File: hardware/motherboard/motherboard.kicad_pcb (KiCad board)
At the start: 2 copper layers, 22 parts, among them J1 Conn_01x02, J2 Conn_02x03_Odd_Even, U1 ESP32-WROOM-32, U2 SHTC3, U3 BMP390, U4 TPS62177DQC, U8 NRF24L01_Breakout

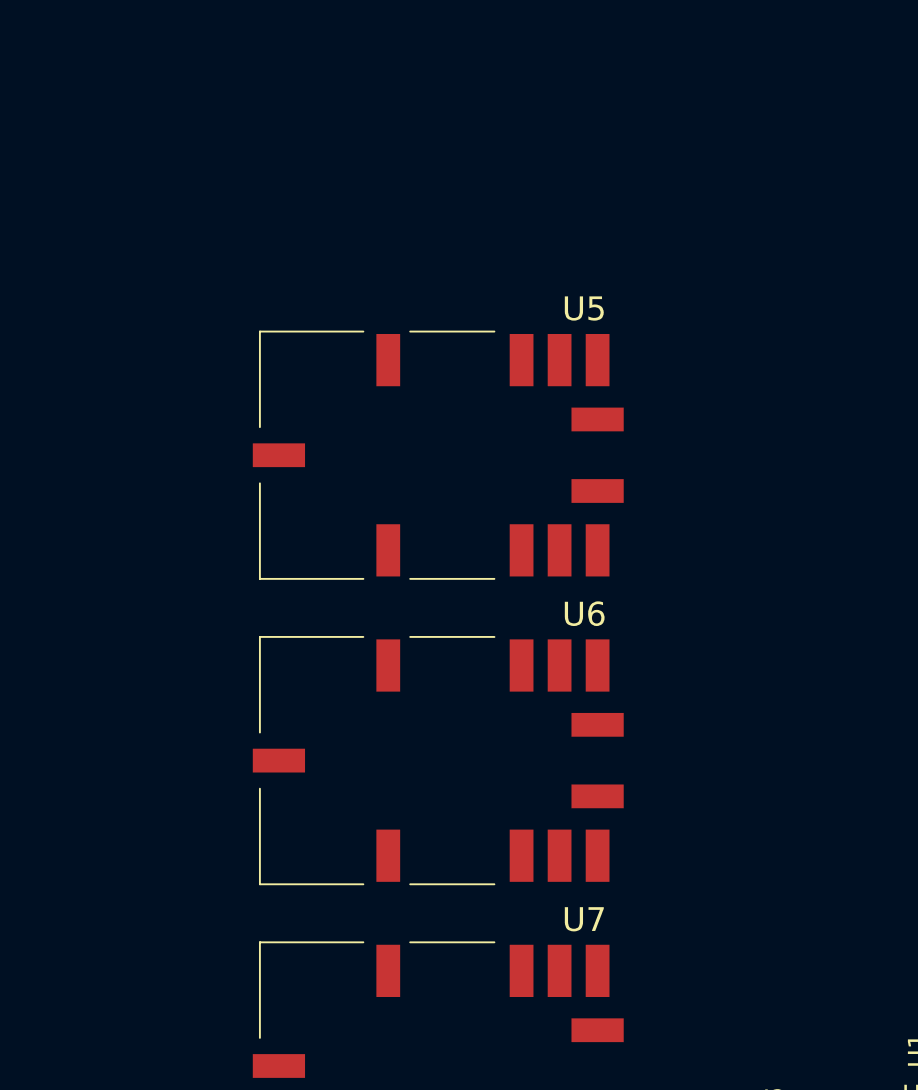
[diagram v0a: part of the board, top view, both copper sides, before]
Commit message: Completed schematic
Completed schematic with all footprints assigned
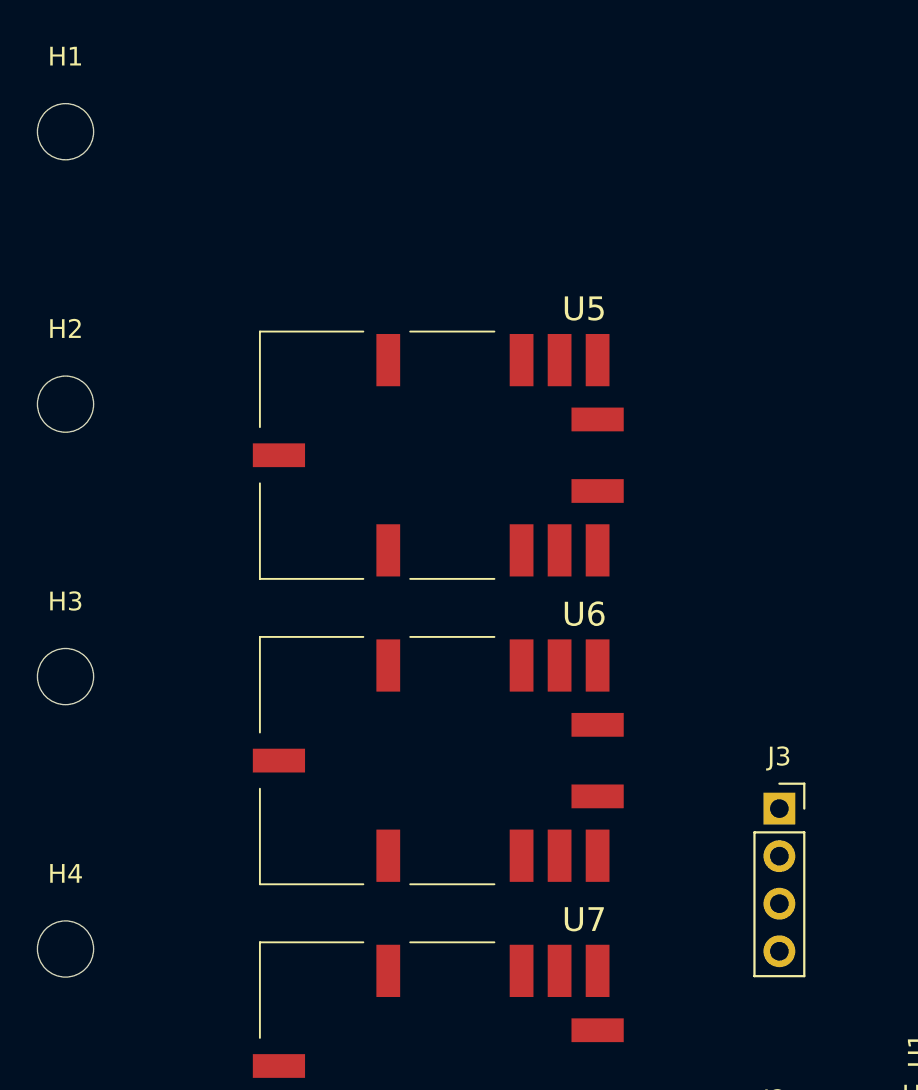
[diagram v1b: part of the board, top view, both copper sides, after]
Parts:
- added H1: MountingHole, MountingHole:MountingHole_3mm, F.Cu at (94.0, 59.1)
- added H2: MountingHole, MountingHole:MountingHole_3mm, F.Cu at (94.0, 73.7)
- added H3: MountingHole, MountingHole:MountingHole_3mm, F.Cu at (94.0, 88.2)
- added H4: MountingHole, MountingHole:MountingHole_3mm, F.Cu at (94.0, 102.8)
- added J3: Conn_01x04, Connector_PinSocket_2.54mm:PinSocket_1x04_P2.54mm_Vertical, F.Cu at (132.1, 95.3)
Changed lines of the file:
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@@
   (net 63 "unconnected-(U7-DNC-Pad7)")
   (net 64 "Net-(J1-Pin_2)")
+  (footprint "MountingHole:MountingHole_3mm" (layer "F.Cu")
+    (at 93.98 73.66)
+    (descr "Mounting Hole 3mm, no annular")
+    (tags "mounting hole 3mm no annular")
+    (property "Sheetfile" "motherboard.kicad_sch")
+    (property "Sheetname" "")
+    (property "ki_description" "Mounting Hole without connection")
+    (property "ki_keywords" "mounting hole")
+    (attr exclude_from_pos_files)
+    (fp_text reference "H2" (at 0 -4) (layer "F.SilkS")
+        (effects (font (size 1 1) (thickness 0.15)))
+    )
+    (fp_text value "MountingHole" (at 0 4) (layer "F.Fab")
+        (effects (font (size 1 1) (thickness 0.15)))
+    )
+    (fp_text user "${REFERENCE}" (at 0 0) (layer "F.Fab")
+        (effects (font (size 1 1) (thickness 0.15)))
+    )
+    (fp_circle (center 0 0) (end 3 0)
+      (stroke (width 0.15) (type solid)) (fill none) (layer "Cmts.User"))
+    (fp_circle (center 0 0) (end 3.25 0)
+      (stroke (width 0.05) (type solid)) (fill none) (layer "F.CrtYd"))
+    (pad "" np_thru_hole circle (at 0 0) (size 3 3) (drill 3) (layers "*.Cu" "*.Mask"))
+  )
   (footprint "Connector_IDC:IDC-Header_2x03_P2.54mm_Vertical" (layer "F.Cu")
     (at 130.5818 116.897874)
@@
       ))
   )
+  (footprint "Connector_PinSocket_2.54mm:PinSocket_1x04_P2.54mm_Vertical" (layer "F.Cu")
+    (at 132.105 95.26)
+    (descr "Through hole straight socket strip, 1x04, 2.54mm pitch, single row (from Kicad 4.0.7), script generated")
+    (tags "Through hole socket strip THT 1x04 2.54mm single row")
+    (property "Sheetfile" "motherboard.kicad_sch")
+    (property "Sheetname" "")
+    (property "ki_description" "Generic connector, single row, 01x04, script generated (kicad-library-utils/schlib/autogen/connector/)")
+    (property "ki_keywords" "connector")
+    (attr through_hole)
+    (fp_text reference "J3" (at 0 -2.77) (layer "F.SilkS")
+        (effects (font (size 1 1) (thickness 0.15)))
+    )
+    (fp_text value "Conn_01x04" (at 0 10.39) (layer "F.Fab")
+        (effects (font (size 1 1) (thickness 0.15)))
+    )
+    (fp_text user "${REFERENCE}" (at 0 3.81 90) (layer "F.Fab")
+        (effects (font (size 1 1) (thickness 0.15)))
+    )
+    (fp_line (start -1.33 1.27) (end -1.33 8.95)
+      (stroke (width 0.12) (type solid)) (layer "F.SilkS"))
+    (fp_line (start -1.33 1.27) (end 1.33 1.27)
+      (stroke (width 0.12) (type solid)) (layer "F.SilkS"))
+    (fp_line (start -1.33 8.95) (end 1.33 8.95)
+      (stroke (width 0.12) (type solid)) (layer "F.SilkS"))
+    (fp_line (start 0 -1.33) (end 1.33 -1.33)
+      (stroke (width 0.12) (type solid)) (layer "F.SilkS"))
+    (fp_line (start 1.33 -1.33) (end 1.33 0)
+      (stroke (width 0.12) (type solid)) (layer "F.SilkS"))
+    (fp_line (start 1.33 1.27) (end 1.33 8.95)
+      (stroke (width 0.12) (type solid)) (layer "F.SilkS"))
+    (fp_line (start -1.8 -1.8) (end 1.75 -1.8)
+      (stroke (width 0.05) (type solid)) (layer "F.CrtYd"))
+    (fp_line (start -1.8 9.4) (end -1.8 -1.8)
+      (stroke (width 0.05) (type solid)) (layer "F.CrtYd"))
+    (fp_line (start 1.75 -1.8) (end 1.75 9.4)
+      (stroke (width 0.05) (type solid)) (layer "F.CrtYd"))
+    (fp_line (start 1.75 9.4) (end -1.8 9.4)
+      (stroke (width 0.05) (type solid)) (layer "F.CrtYd"))
+    (fp_line (start -1.27 -1.27) (end 0.635 -1.27)
+      (stroke (width 0.1) (type solid)) (layer "F.Fab"))
+    (fp_line (start -1.27 8.89) (end -1.27 -1.27)
+      (stroke (width 0.1) (type solid)) (layer "F.Fab"))
+    (fp_line (start 0.635 -1.27) (end 1.27 -0.635)
+      (stroke (width 0.1) (type solid)) (layer "F.Fab"))
+    (fp_line (start 1.27 -0.635) (end 1.27 8.89)
+      (stroke (width 0.1) (type solid)) (layer "F.Fab"))
+    (fp_line (start 1.27 8.89) (end -1.27 8.89)
+      (stroke (width 0.1) (type solid)) (layer "F.Fab"))
+    (pad "1" thru_hole rect (at 0 0) (size 1.7 1.7) (drill 1) (layers "*.Cu" "*.Mask")
+      (net 1 "GND") (pinfunction "Pin_1") (pintype "passive"))
+    (pad "2" thru_hole oval (at 0 2.54) (size 1.7 1.7) (drill 1) (layers "*.Cu" "*.Mask")
+      (net 3 "+3.3V") (pinfunction "Pin_2") (pintype "passive"))
+    (pad "3" thru_hole oval (at 0 5.08) (size 1.7 1.7) (drill 1) (layers "*.Cu" "*.Mask")
+      (net 48 "/SDA") (pinfunction "Pin_3") (pintype "passive"))
+    (pad "4" thru_hole oval (at 0 7.62) (size 1.7 1.7) (drill 1) (layers "*.Cu" "*.Mask")
+      (net 49 "/SCL") (pinfunction "Pin_4") (pintype "passive"))
+    (model "${KICAD6_3DMODEL_DIR}/Connector_PinSocket_2.54mm.3dshapes/PinSocket_1x04_P2.54mm_Vertical.wrl"
+      (offset (xyz 0 0 0))
+      (scale (xyz 1 1 1))
+      (rotate (xyz 0 0 0))
+    )
+  )
   (footprint "Jumper:SolderJumper-2_P1.3mm_Open_RoundedPad1.0x1.5mm" (layer "F.Cu")
     (at 113.3068 126.037874)
@@
       ))
   )
+  (footprint "MountingHole:MountingHole_3mm" (layer "F.Cu")
+    (at 93.98 102.76)
+    (descr "Mounting Hole 3mm, no annular")
+    (tags "mounting hole 3mm no annular")
+    (property "Sheetfile" "motherboard.kicad_sch")
+    (property "Sheetname" "")
+    (property "ki_description" "Mounting Hole without connection")
+    (property "ki_keywords" "mounting hole")
+    (attr exclude_from_pos_files)
+    (fp_text reference "H4" (at 0 -4) (layer "F.SilkS")
+        (effects (font (size 1 1) (thickness 0.15)))
+    )
+    (fp_text value "MountingHole" (at 0 4) (layer "F.Fab")
+        (effects (font (size 1 1) (thickness 0.15)))
+    )
+    (fp_text user "${REFERENCE}" (at 0 0) (layer "F.Fab")
+        (effects (font (size 1 1) (thickness 0.15)))
+    )
+    (fp_circle (center 0 0) (end 3 0)
+      (stroke (width 0.15) (type solid)) (fill none) (layer "Cmts.User"))
+    (fp_circle (center 0 0) (end 3.25 0)
+      (stroke (width 0.05) (type solid)) (fill none) (layer "F.CrtYd"))
+    (pad "" np_thru_hole circle (at 0 0) (size 3 3) (drill 3) (layers "*.Cu" "*.Mask"))
+  )
   (footprint "Connector_AMASS:AMASS_XT60-F_1x02_P7.20mm_Vertical" (layer "F.Cu")
     (at 142.4968 132.697874)
@@
       (rotate (xyz 0 0 0))
     )
+  )
+  (footprint "MountingHole:MountingHole_3mm" (layer "F.Cu")
+    (at 93.98 88.21)
+    (descr "Mounting Hole 3mm, no annular")
+    (tags "mounting hole 3mm no annular")
+    (property "Sheetfile" "motherboard.kicad_sch")
+    (property "Sheetname" "")
+    (property "ki_description" "Mounting Hole without connection")
+    (property "ki_keywords" "mounting hole")
+    (attr exclude_from_pos_files)
+    (fp_text reference "H3" (at 0 -4) (layer "F.SilkS")
+        (effects (font (size 1 1) (thickness 0.15)))
+    )
+    (fp_text value "MountingHole" (at 0 4) (layer "F.Fab")
+        (effects (font (size 1 1) (thickness 0.15)))
+    )
+    (fp_text user "${REFERENCE}" (at 0 0) (layer "F.Fab")
+        (effects (font (size 1 1) (thickness 0.15)))
+    )
+    (fp_circle (center 0 0) (end 3 0)
+      (stroke (width 0.15) (type solid)) (fill none) (layer "Cmts.User"))
+    (fp_circle (center 0 0) (end 3.25 0)
+      (stroke (width 0.05) (type solid)) (fill none) (layer "F.CrtYd"))
+    (pad "" np_thru_hole circle (at 0 0) (size 3 3) (drill 3) (layers "*.Cu" "*.Mask"))
   )
   (footprint "RF_Module:ESP32-WROOM-32D" (layer "F.Cu")
@@
       ))
   )
+  (footprint "MountingHole:MountingHole_3mm" (layer "F.Cu")
+    (at 93.98 59.11)
+    (descr "Mounting Hole 3mm, no annular")
+    (tags "mounting hole 3mm no annular")
+    (property "Sheetfile" "motherboard.kicad_sch")
+    (property "Sheetname" "")
+    (property "ki_description" "Mounting Hole without connection")
+    (property "ki_keywords" "mounting hole")
+    (attr exclude_from_pos_files)
+    (fp_text reference "H1" (at 0 -4) (layer "F.SilkS")
+        (effects (font (size 1 1) (thickness 0.15)))
+    )
+    (fp_text value "MountingHole" (at 0 4) (layer "F.Fab")
+        (effects (font (size 1 1) (thickness 0.15)))
+    )
+    (fp_text user "${REFERENCE}" (at 0 0) (layer "F.Fab")
+        (effects (font (size 1 1) (thickness 0.15)))
+    )
+    (fp_circle (center 0 0) (end 3 0)
+      (stroke (width 0.15) (type solid)) (fill none) (layer "Cmts.User"))
+    (fp_circle (center 0 0) (end 3.25 0)
+      (stroke (width 0.05) (type solid)) (fill none) (layer "F.CrtYd"))
+    (pad "" np_thru_hole circle (at 0 0) (size 3 3) (drill 3) (layers "*.Cu" "*.Mask"))
+  )
   (footprint "RF_Module:nRF24L01_Breakout" (layer "F.Cu")

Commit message: Initial PCB design
Initial PCB design complete
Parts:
- added C1: 100n, Capacitor_SMD:C_0603_1608Metric, F.Cu at (142.6, 121.6)
- added C10: 100n, Capacitor_SMD:C_0603_1608Metric, F.Cu at (168.0, 118.6)
- added C2: 100n, Capacitor_SMD:C_0603_1608Metric, F.Cu at (142.6, 123.1)
- added C3: 100n, Capacitor_SMD:C_0603_1608Metric, F.Cu at (156.8, 112.9)
- added C4: 2.2u, Capacitor_SMD:C_0603_1608Metric, F.Cu at (149.9, 125.4)
- added C5: 22u, Capacitor_SMD:C_0805_2012Metric, F.Cu at (156.4, 121.8)
- added C6: 100n, Capacitor_SMD:C_0603_1608Metric, F.Cu at (168.0, 120.3)
- added C7: 100n, Capacitor_SMD:C_0603_1608Metric, F.Cu at (168.0, 121.9)
- added C8: 10u, Capacitor_SMD:C_0805_2012Metric, F.Cu at (136.3, 94.7)
- added C9: 100n, Capacitor_SMD:C_0603_1608Metric, F.Cu at (136.4, 92.7)
- added D1: LED, LED_SMD:LED_0805_2012Metric, F.Cu at (136.9, 112.3)
- added D2: LED, LED_SMD:LED_0805_2012Metric, F.Cu at (145.7, 113.6)
- added D3: LED, LED_SMD:LED_0805_2012Metric, F.Cu at (136.9, 110.1)
- added D4: LED, LED_SMD:LED_0805_2012Metric, F.Cu at (148.0, 113.7)
- added L1: 10u, Inductor_SMD:L_Taiyo-Yuden_MD-4040, F.Cu at (158.5, 125.6)
- added R1: 4.7k, Resistor_SMD:R_0603_1608Metric, F.Cu at (138.6, 119.3)
- added R10: 130R, Resistor_SMD:R_0603_1608Metric, F.Cu at (145.7, 117.1)
- added R11: 130R, Resistor_SMD:R_0603_1608Metric, F.Cu at (133.0, 110.1)
- added R12: 130R, Resistor_SMD:R_0603_1608Metric, F.Cu at (148.0, 117.1)
- added R13: 10k, Resistor_SMD:R_0603_1608Metric, F.Cu at (136.5, 105.7)
- added R14: 10k, Resistor_SMD:R_0603_1608Metric, F.Cu at (136.5, 100.7)
- added R2: 4.7k, Resistor_SMD:R_0603_1608Metric, F.Cu at (135.0, 122.3)
- added R3: 10k, Resistor_SMD:R_0603_1608Metric, F.Cu at (159.6, 114.7)
- added R4: 10k, Resistor_SMD:R_0603_1608Metric, F.Cu at (154.1, 114.7)
- added R6: 10k, Resistor_SMD:R_0603_1608Metric, F.Cu at (136.5, 104.0)
- added R7: 20k, Resistor_SMD:R_0603_1608Metric, F.Cu at (153.5, 128.7)
- added R8: 10k, Resistor_SMD:R_0603_1608Metric, F.Cu at (153.5, 130.7)
- added R9: 130R, Resistor_SMD:R_0603_1608Metric, F.Cu at (133.0, 112.3)
- moved U5 80.5 mm to (191.3, 98.6)
- moved U6 80.4 mm to (191.3, 114.4)
- moved U7 80.3 mm to (191.3, 130.3)
- moved JP2 78.1 mm to (176.5, 92.1), turned to 180 degrees
- moved JP3 77.3 mm to (176.5, 97.7), turned to 180 degrees
- moved JP1 75.8 mm to (176.5, 94.9), turned to 180 degrees
- moved JP4 70.0 mm to (176.5, 100.5), turned to 180 degrees
- moved H1 69.9 mm to (24.6, 67.6)
- moved H2 69.9 mm to (24.6, 82.1)
- moved H3 69.9 mm to (24.6, 96.7)
- moved H4 69.9 mm to (24.6, 111.2)
- moved JP5 68.4 mm to (176.5, 111.6), turned to 180 degrees
- moved JP6 68.2 mm to (176.5, 117.2), turned to 180 degrees
- moved JP8 64.7 mm to (176.5, 108.8), turned to 180 degrees
- moved JP9 64.3 mm to (176.5, 114.4), turned to 180 degrees
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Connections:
- U1 pad 10: unconnected-(U1-IO25-Pad10) -> /nRST
- U4 pad 7: Net-(U4-PG) -> unconnected-(U4-PG-Pad7)
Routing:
- net +3.3V: track 0.00 -> 101.0 mm, vias 0 -> 8
- net +3.3VP: track 0.00 -> 79.1 mm, vias 0 -> 2
- net /MOSI: track 0.00 -> 71.3 mm, vias 0 -> 2
- net /SCL: track 0.00 -> 67.2 mm, vias 0 -> 2
- net /MISO: track 0.00 -> 65.5 mm, vias 0 -> 2
- net /MISO_S: track 0.00 -> 64.7 mm
- net /SDA: track 0.00 -> 62.0 mm, vias 0 -> 5
- net /nSS_{1}: track 0.00 -> 60.9 mm, vias 0 -> 4
- net /MOSI_S: track 0.00 -> 60.1 mm
- net /SCK_S: track 0.00 -> 57.2 mm
- net /nRST_S: track 0.00 -> 55.9 mm, vias 0 -> 6
- net /DAV_{3}: track 0.00 -> 53.6 mm, vias 0 -> 2
- net /SCK: track 0.00 -> 52.0 mm, vias 0 -> 2
- net /nSS_{3}: track 0.00 -> 49.4 mm, vias 0 -> 4
- net /DAV_{1}: track 0.00 -> 48.0 mm, vias 0 -> 2
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- added copper zone on F.Cu, net +3.3V
- added copper zone on F.Cu, net GND
- added copper zone on F.Cu, net GND1
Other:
- board outline added: 74.8 x 50.9 mm

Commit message: Finalized PCB design revision 1
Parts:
- moved H2 189.6 mm to (205.8, 138.3)
- moved H3 181.3 mm to (205.7, 88.2)
- moved H4 107.6 mm to (128.8, 138.2)
- moved H1 106.1 mm to (128.7, 88.2)
- moved C7 41.1 mm to (203.6, 101.3), turned to -90 degrees
- moved C6 36.9 mm to (203.6, 130.2), turned to -90 degrees
- moved C10 35.6 mm to (203.5, 116.1), turned to -90 degrees
- moved C5 5.78 mm to (150.8, 123.3), turned to -90 degrees
- moved C4 0.92 mm to (149.0, 125.4)
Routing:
- net +3.3V: track 101.0 -> 55.8 mm, vias 8 -> 4
- net GND: track 25.9 -> 58.8 mm, vias 2 -> 5
- net Net-(J1-Pin_2): track 16.3 -> 0.00 mm
- net +3.3VP: track 79.1 -> 85.9 mm, vias 2 -> 4
- net Net-(U4-SW): track 5.84 -> 0.00 mm
- net /MISO: track 65.5 -> 60.3 mm
- net /MISO_S: track 64.7 -> 66.6 mm, vias 0 -> 2
- net /nSS_{1}: track 60.9 -> 62.0 mm
- net /nRST: track 43.1 -> 44.0 mm
- net /nSS_{2}_S: track 24.0 -> 23.4 mm
- net /SCL: track 67.2 -> 67.0 mm, vias 2 -> 4
- net /SDA: track 62.0 -> 62.1 mm, vias 5 -> 4
- net /nRST_S: track 55.9 -> 56.0 mm, vias 6 -> 4
- net /MOSI_S: vias 0 -> 2
- added copper zone on B.Cu, net +3.3V
- added copper zone on F.Cu, net Net-(J1-Pin_2)
- added copper zone on F.Cu, net Net-(U4-SW)
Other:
- board size 74.8 x 50.9 mm -> 83.7 x 56.7 mm
- board text added: "3"
- board text added: "C"
- board text added: "D"
- board text added: "G"

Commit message: Hole change
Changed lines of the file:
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@@
     (fp_line (start 5.72 10.18) (end -3.18 10.18)
       (stroke (width 0.1) (type solid)) (layer "F.Fab"))
-    (pad "1" thru_hole roundrect (at 0 0) (size 1.7 1.7) (drill 1) (layers "*.Cu" "*.Mask") (roundrect_rratio 0.147059)
+    (pad "1" thru_hole roundrect (at 0 0) (size 1.7 1.7) (drill 1) (layers "*.Cu" "*.Mask") (roundrect_rratio 0.1470588235)
       (net 2 "/EN") (pinfunction "Pin_1") (pintype "passive"))
     (pad "2" thru_hole circle (at 2.54 0) (size 1.7 1.7) (drill 1) (layers "*.Cu" "*.Mask")
